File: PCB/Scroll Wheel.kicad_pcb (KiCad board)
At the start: 2 copper layers, 39.4 x 60.5 mm, 39 parts, among them J1 TC2030, J2 USB_C_Receptacle_USB3.1_16P, J3 Conn_01x02_Pin, J4 Connector Encoder, J5 Connector controller, Q2 BC847, Q3 FDC6318P, SW1 SW_Push, U1 ESP32-WROOM-E, U2 BQ25172DSGR, U6 MIC5504-3.3YM5, U7 AS5600

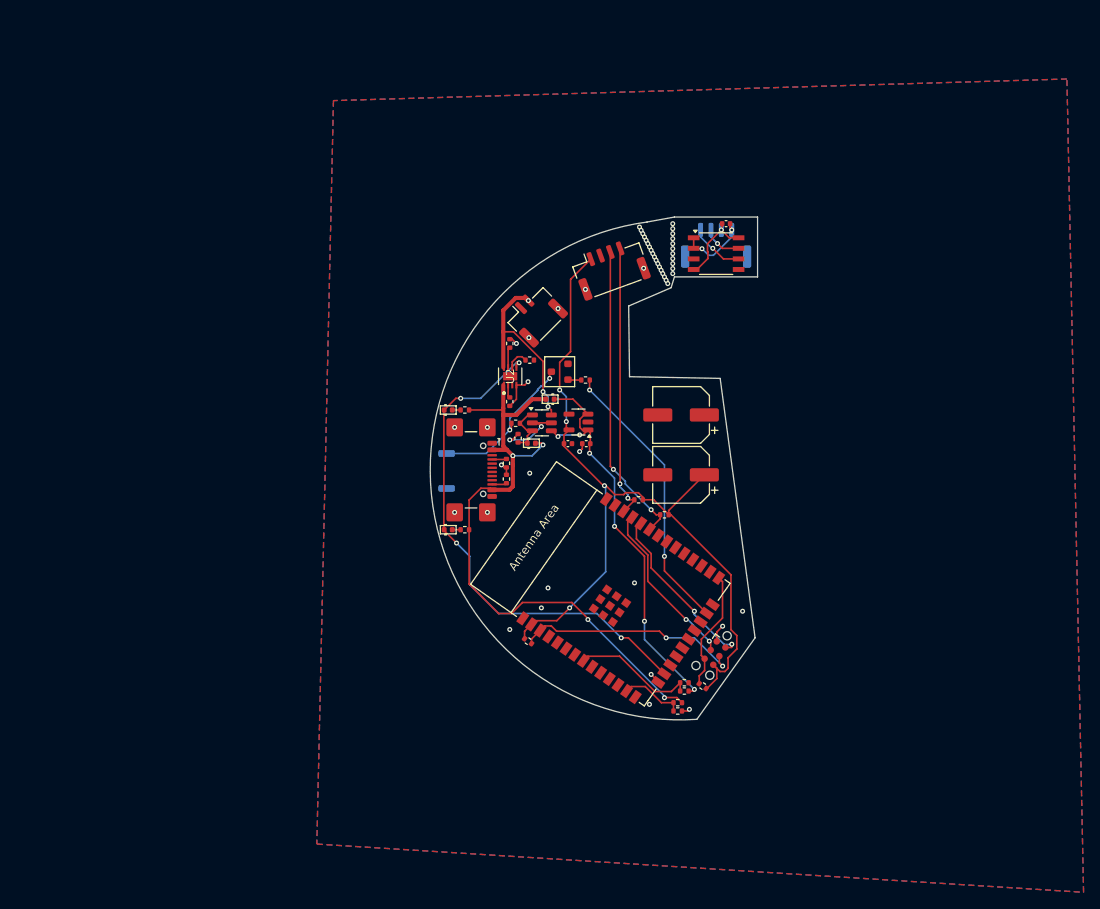
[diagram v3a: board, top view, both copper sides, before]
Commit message: Complete rerouting, fixing all open issues #6 #2 #1
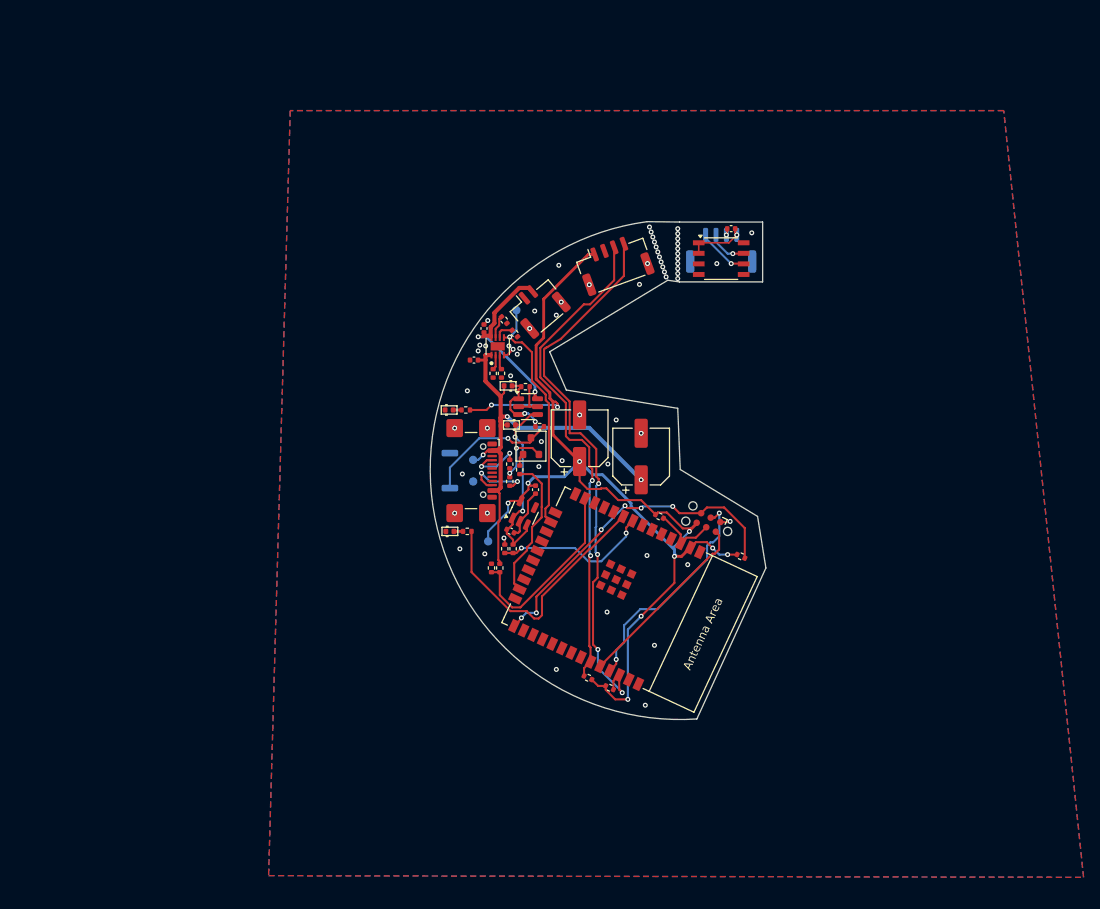
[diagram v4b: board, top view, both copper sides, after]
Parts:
- removed D1, D4: LED, PCM_Diode_SMD_AKL:D_0402_1005Metric
- removed R19, R25: 1k, Resistor_SMD:R_0402_1005Metric
- added C1: 22uF, Capacitor_SMD:C_0402_1005Metric, F.Cu at (102.7, 55.0)
- added C3: 22uF, Capacitor_SMD:C_0402_1005Metric, F.Cu at (101.5, 58.8)
- added D2: LED, PCM_Diode_SMD_AKL:D_0402_1005Metric, F.Cu at (98.6, 79.4)
- added D6: LED, PCM_Diode_SMD_AKL:D_0402_1005Metric, F.Cu at (98.5, 64.8)
- added R1: 150, Resistor_SMD:R_0402_1005Metric, F.Cu at (100.7, 79.4)
- added R2: 150, Resistor_SMD:R_0402_1005Metric, F.Cu at (100.5, 64.8)
- added R3: 5.1k, Resistor_SMD:R_0402_1005Metric, F.Cu at (104.8, 60.4)
- added TP1: VDC, TestPoint:TestPoint_Pad_D1.0mm, B.Cu at (101.4, 70.8)
- added TP2: GND, TestPoint:TestPoint_Pad_D1.0mm, B.Cu at (101.4, 73.4)
- added TP3: 3.3V, TestPoint:TestPoint_Pad_D1.0mm, B.Cu at (103.2, 80.6)
- added TP5: State, TestPoint:TestPoint_Pad_D1.0mm, B.Cu at (106.6, 52.8)
- R17: value 330 -> 680
- moved R24 28.2 mm to (103.6, 83.8), turned to -90 degrees
- moved R12 26.9 mm to (105.2, 81.5), turned to -90 degrees
- moved R9 26.8 mm to (104.6, 83.8), turned to 90 degrees
- moved R8 26.8 mm to (106.2, 81.5), turned to 90 degrees
- moved R15 22.9 mm to (117.8, 98.2), turned to 155 degrees
- moved R13 21.8 mm to (123.8, 77.6), turned to 155 degrees
- moved R16 21.7 mm to (115.2, 97.0), turned to -25 degrees
- moved R14 16.3 mm to (133.6, 82.4), turned to -25 degrees
- moved J1 15.7 mm to (129.7, 78.3), turned to 155 degrees
- moved C9 13.9 mm to (105.9, 79.4), turned to 155 degrees
- moved R28 13.4 mm to (107.0, 72.0), turned to 90 degrees
- moved C5 13.0 mm to (114.2, 68.2), turned to 90 degrees
- moved U6 12.7 mm to (107.5, 77.2), turned to 65 degrees
- moved Q2 9.59 mm to (108.3, 69.2), turned to 90 degrees
- moved D5 7.45 mm to (105.6, 61.9), turned to 180 degrees
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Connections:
- C11 pad 1: Net-(J4-Pin_2) -> GND
- C7 pad 1: +5V -> VDC
- J3 pad MP: (no net) -> GND
- J4 pad 2: Net-(J4-Pin_2) -> GND
- J4 pad MP: (no net) -> GND
- J5 pad MP: (no net) -> GND
- U1 pad 34: unconnected-(U1-U0RXD/GPIO3-Pad34) -> RX
- U1 pad 9: unconnected-(U1-32K_XN/GPIO33/ADC1_CH5-Pad9) -> LED
- U2 pad 3: unconnected-(U2-TS-Pad3) -> Net-(U2-TS)
- U7 pad 4: Net-(J4-Pin_2) -> GND
- U7 pad 8: Net-(J4-Pin_2) -> GND
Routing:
- net +3.3V: track 100.2 -> 136.2 mm, vias 4 -> 11
- net SDA: track 33.2 -> 68.0 mm, vias 2 -> 4
- net STATE: track 62.5 -> 29.4 mm, vias 4 -> 1
- net LED: track 0.00 -> 31.9 mm
- net BATT_sense_high: track 51.0 -> 22.4 mm, vias 6 -> 2
- net BOOT: track 14.4 -> 40.6 mm, vias 0 -> 6
- net SCL: track 36.7 -> 59.7 mm
- net VDC: track 78.8 -> 56.2 mm, vias 4 -> 3
- net EN: track 27.5 -> 7.83 mm, vias 2 -> 0
- net PWR_sw: track 33.9 -> 17.5 mm, vias 2 -> 0
- net PWR_sense: track 7.67 -> 23.2 mm
- net Net-(J4-Pin_2): track 9.66 -> 0.00 mm, vias 1 -> 0
- net TX: track 20.4 -> 27.1 mm
- net Net-(J2-CC2): track 1.83 -> 8.22 mm, vias 0 -> 2
- net Net-(U6-GND): track 1.08 -> 6.08 mm, vias 1 -> 0
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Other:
- board size 39.4 x 60.5 mm -> 40.4 x 59.9 mm
- board text added: "V2.4"
- board text removed: "V2.3"

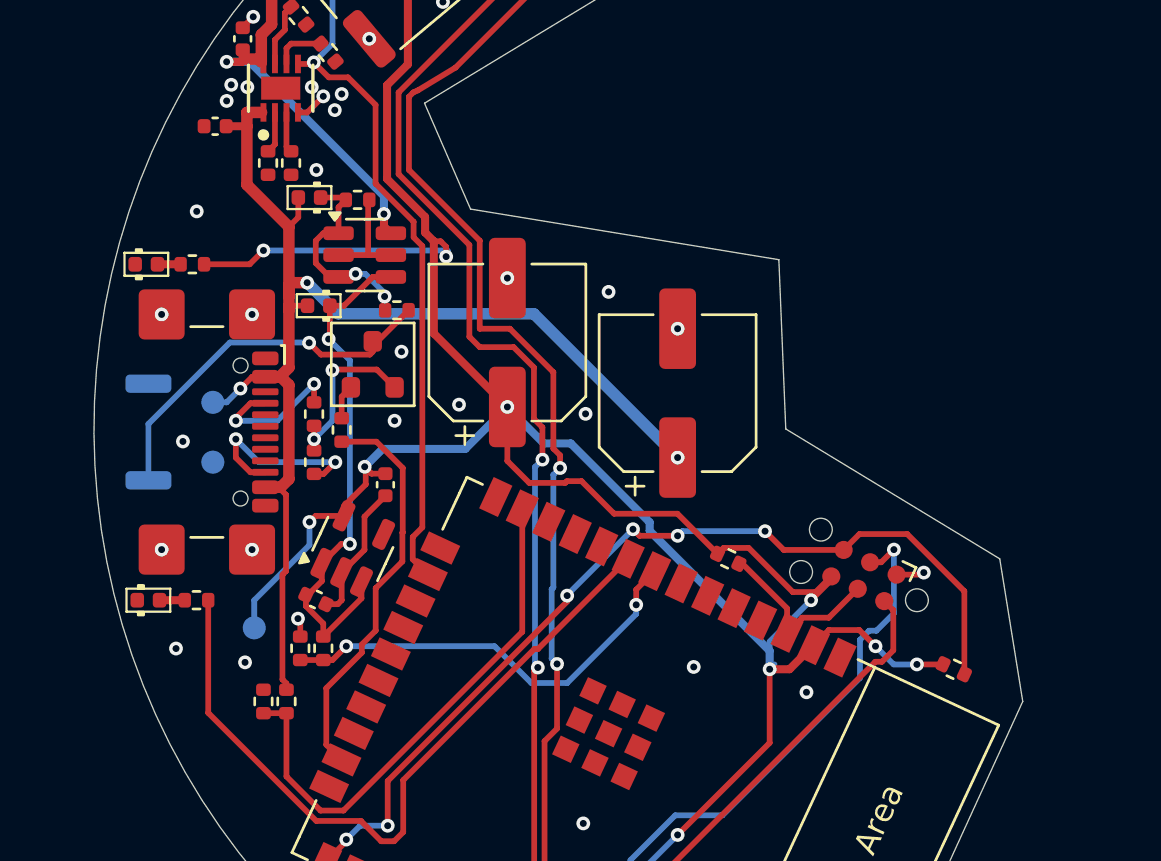
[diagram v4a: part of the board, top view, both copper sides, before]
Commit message: add a better mounting solution
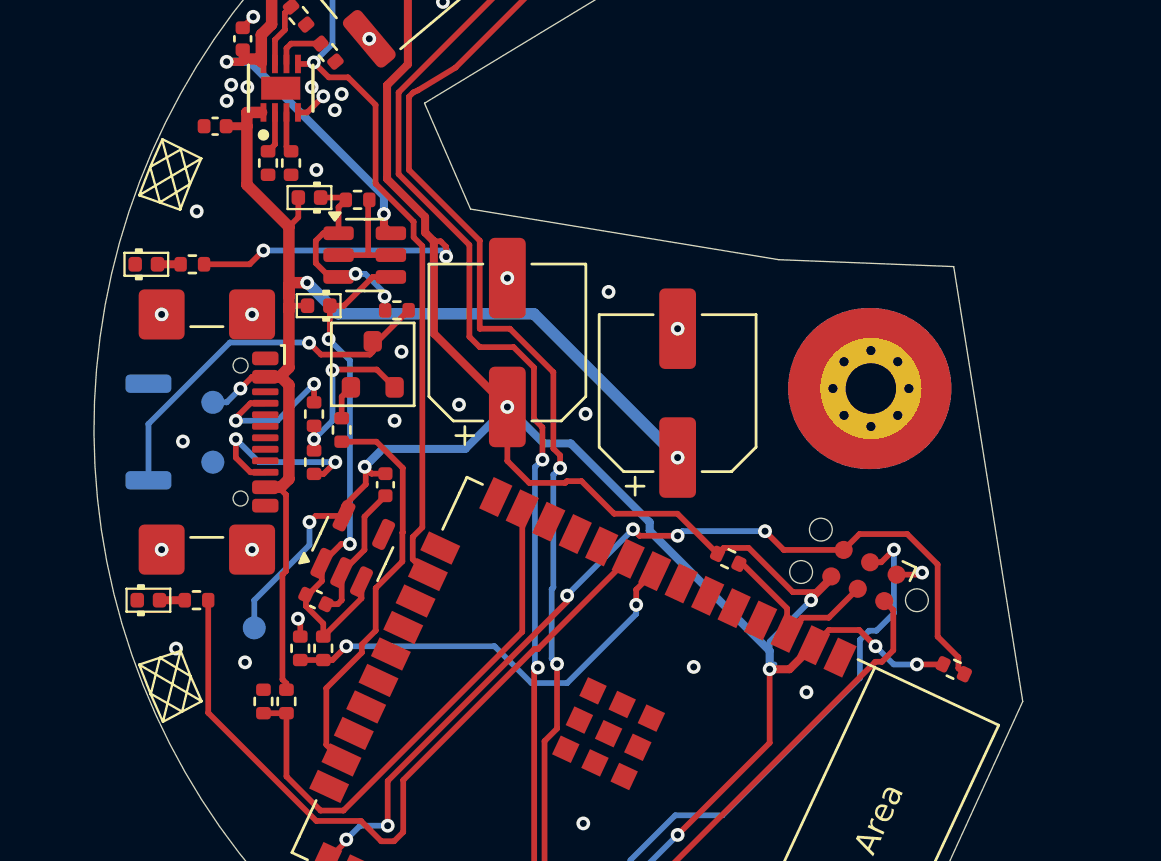
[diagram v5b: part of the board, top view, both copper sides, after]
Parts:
- added REF**: MountingHole_2.2mm_M2_Pad_Via, MountingHole:MountingHole_2.2mm_M2_Pad_Via, F.Cu at (130.0, 70.2)
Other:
- outline, holes or cut-outs redrawn
